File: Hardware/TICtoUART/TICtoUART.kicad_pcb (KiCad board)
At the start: 2 copper layers, 54.9 x 41.3 mm, 13 parts, among them J1 Conn_01x02_Male, J2 Conn_01x03_Male, J3 Conn_01x02_Male, U1 SFH617A-2X009T, U2 LM358

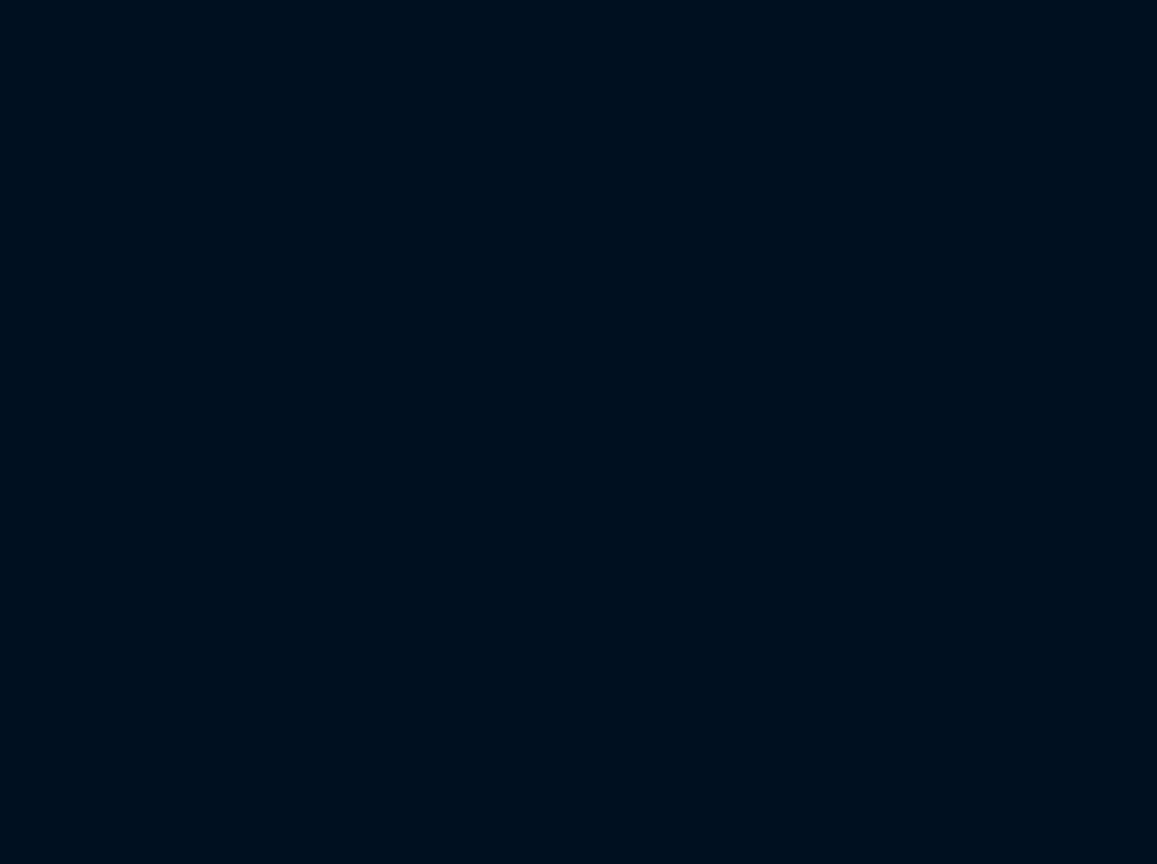
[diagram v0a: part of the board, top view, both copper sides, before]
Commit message: added MQTT + status LED
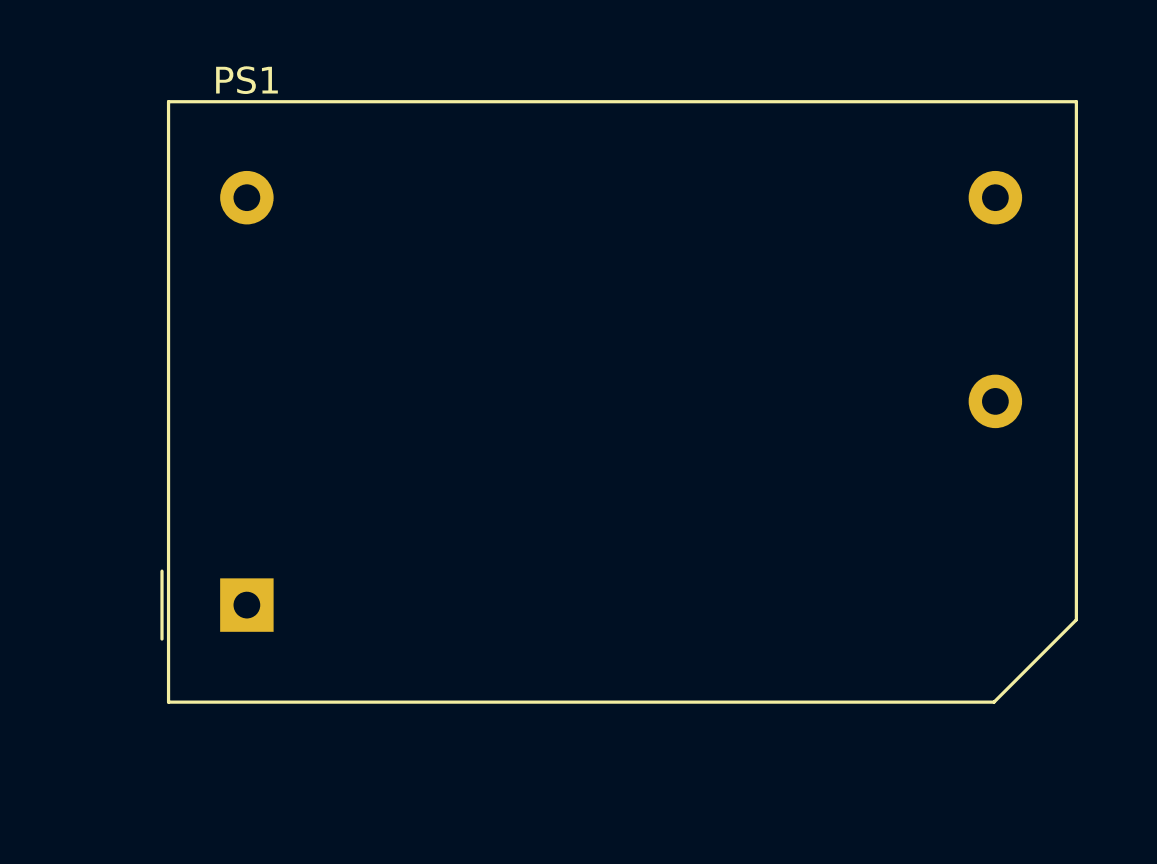
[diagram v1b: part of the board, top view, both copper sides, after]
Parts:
- added PS1: RAC01-05SGB, Converter_ACDC:Converter_ACDC_RECOM_RAC01-xxSGB_THT, F.Cu at (119.4, 61.0)
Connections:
- R2 pad 1: +5V -> +3V3
- R3 pad 1: +5V -> +3V3
- RV1 pad 1: +5V -> +3V3
- U2 pad 8: +5V -> +3V3
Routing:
- net +5V: track 38.6 -> 0.00 mm
- net +3V3: track 0.00 -> 38.6 mm

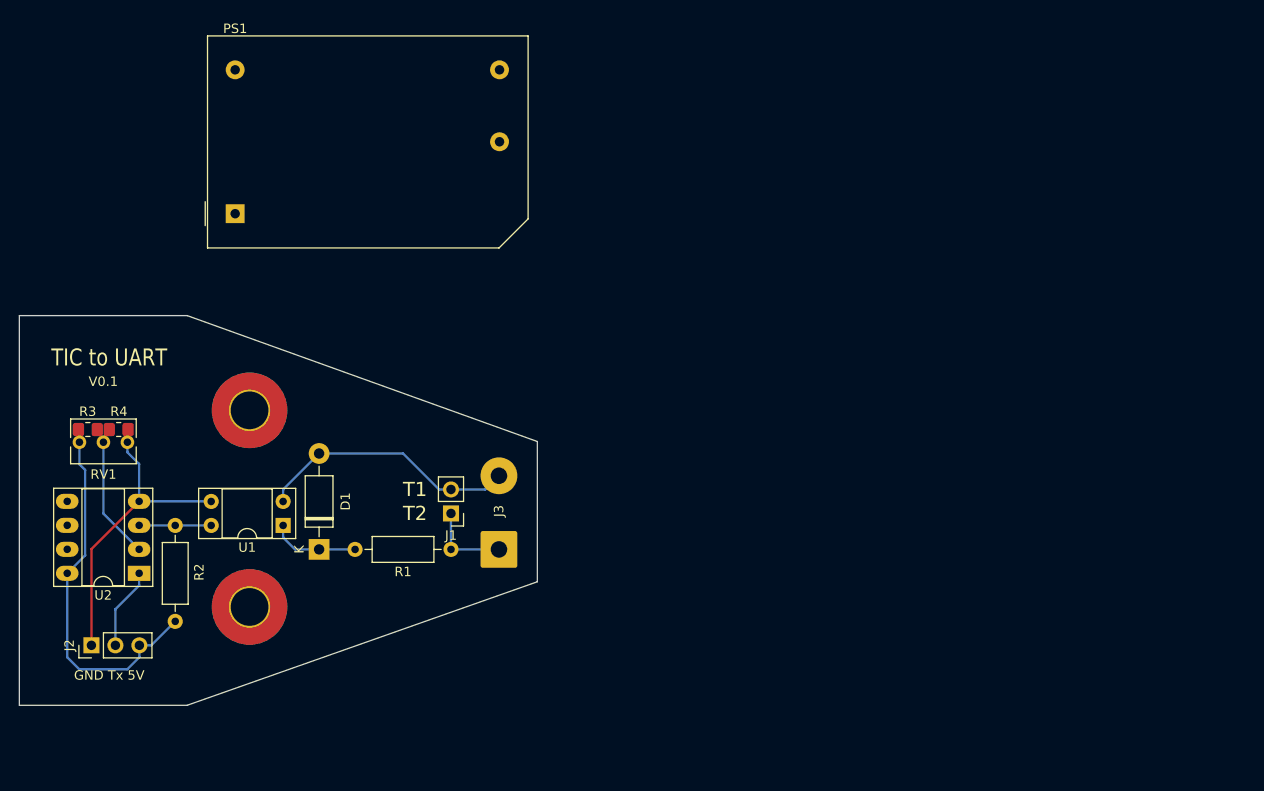
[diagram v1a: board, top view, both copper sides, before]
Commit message: Fully reworked PCB to host an ESP32 devkit Added CAD for enclosuer
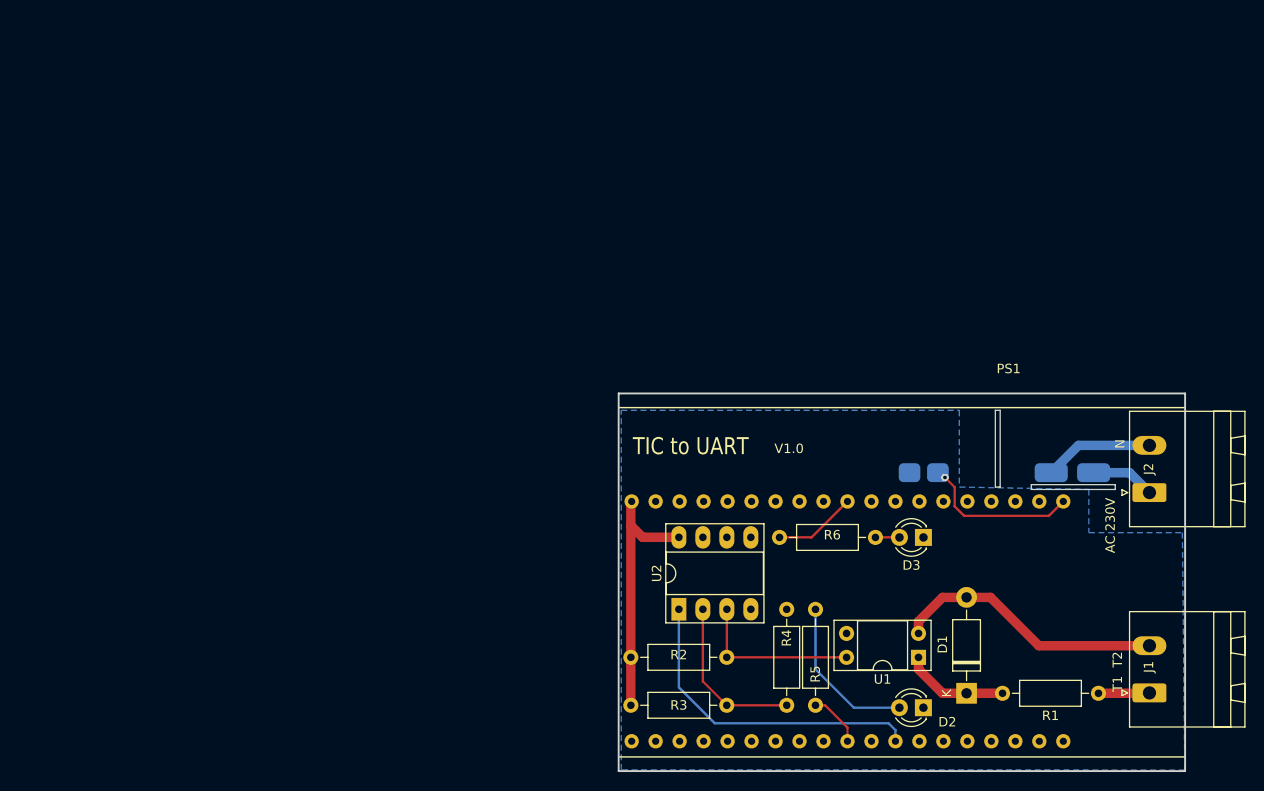
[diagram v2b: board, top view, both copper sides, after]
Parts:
- removed J3: Conn_01x02_Male, Connector_Wire:SolderWire-1sqmm_1x02_P7.8mm_D1.4mm_OD3.9mm
- removed REF** (x2): MountingHole_4mm_Pad_TopBottom, MountingHole:MountingHole_4mm_Pad_TopBottom
- removed RV1: R_Potentiometer, Potentiometer_THT:Potentiometer_Bourns_3266Y_Vertical
- added D2: Red, LED_THT:LED_D3.0mm, F.Cu at (192.3, 113.3)
- added D3: Blue, LED_THT:LED_D3.0mm, F.Cu at (192.3, 95.2)
- added R5: 65R, Resistor_THT:R_Axial_DIN0207_L6.3mm_D2.5mm_P10.16mm_Horizontal, F.Cu at (180.8, 113.0)
- added R6: 15R, Resistor_THT:R_Axial_DIN0207_L6.3mm_D2.5mm_P10.16mm_Horizontal, F.Cu at (177.0, 95.2)
- added U3: DOIT-ESP32-DEVKIT-V1, doit-esp32-devkit-kicad-master:ESP_WROOM_32-DOIT-DEVKIT, B.Cu at (158.8, 104.1)
- J1: footprint Connector_PinHeader_2.54mm:PinHeader_1x02_P2.54mm_Vertical -> Connector_Phoenix_MSTB:PhoenixContact_MSTBA_2,5_2-G_1x02_P5.00mm_Horizontal
- J2: value Conn_01x03_Male -> Conn_01x02_Female; footprint Connector_PinHeader_2.54mm:PinHeader_1x03_P2.54mm_Vertical -> Connector_Phoenix_MSTB:PhoenixContact_MSTBA_2,5_2-G_1x02_P5.00mm_Horizontal
- PS1: value RAC01-05SGB -> WX-DC12003; footprint Converter_ACDC:Converter_ACDC_RECOM_RAC01-xxSGB_THT -> doit-esp32-devkit-kicad-master:WX-DC12003; moved to B.Cu
- R1: value R -> 1k8
- R3, R4: value R -> 120K; footprint Resistor_SMD:R_0805_2012Metric_Pad1.20x1.40mm_HandSolder -> Resistor_THT:R_Axial_DIN0207_L6.3mm_D2.5mm_P10.16mm_Horizontal
- moved J2 113.2 mm to (216.2, 90.5)
- moved PS1 95.0 mm to (210.3, 88.4), turned to 180 degrees
- moved R4 76.5 mm to (177.8, 113.0), turned to 90 degrees
- moved J1 76.4 mm to (216.2, 111.7), turned to 90 degrees
- moved D1 70.3 mm to (196.8, 111.8)
- moved R1 70.3 mm to (210.8, 111.8)
- moved U1 68.7 mm to (191.8, 108.0)
- moved R3 64.5 mm to (161.3, 113.0)
- moved U2 57.3 mm to (166.4, 102.9), turned to 90 degrees
- moved R2 48.4 mm to (161.3, 108.0), turned to 0 degrees
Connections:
- J2 pad 1: GND -> Net-(PS1-Pad1)
- J2 pad 2: Net-(U2-Pad1) -> Net-(PS1-Pad2)
- PS1 pad 1: Net-(J2-Pad2) -> Net-(PS1-Pad1)
- PS1 pad 2: Net-(J2-Pad1) -> Net-(PS1-Pad2)
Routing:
- net GND: track 31.8 -> 0.00 mm
- net Net-(U2-Pad1): track 8.68 -> 34.3 mm
- net Net-(D2-Pad2): track 0.00 -> 16.9 mm
- net Net-(PS1-Pad4): track 0.00 -> 16.0 mm, vias 0 -> 1
- net Net-(PS1-Pad2): track 0.00 -> 11.6 mm
- net +3V3: track 38.6 -> 27.2 mm
- net Net-(R2-Pad2): track 7.63 -> 17.8 mm
- net Net-(U3-Pad10): track 0.00 -> 8.78 mm
- net Net-(PS1-Pad1): track 0.00 -> 6.78 mm
- net Net-(U3-Pad29): track 0.00 -> 5.81 mm
- net Net-(R3-Pad2): track 12.9 -> 17.6 mm
- net Net-(J1-Pad1): track 8.89 -> 5.42 mm
- net Net-(D3-Pad2): track 0.00 -> 2.54 mm
- net Net-(D1-Pad1): track 9.42 -> 11.2 mm
- net Net-(D1-Pad2): track 27.9 -> 28.9 mm
- added copper zone on B.Cu, net GND
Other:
- board size 54.9 x 41.3 mm -> 60 x 40 mm
- board text added: "AC 230V"
- board text added: "N"
- board text added: "T1 T2"
- board text added: "V1.0"
- board text removed: "GND Tx 5V"
- board text removed: "T1"
- board text removed: "T2"
- board text removed: "V0.1"
